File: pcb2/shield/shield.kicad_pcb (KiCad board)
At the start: 2 copper layers, 48.4 x 50 mm, 17 parts, among them IC1 AM26C31CNSR, IC2 AM26C31CNSR, P1 ARD_NW, P10 BUS5, P11 BUS6, P12 BUS7, P13 BUS8, P2 ARD_SW, P3 ARD_NE, P4 ARD_SE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

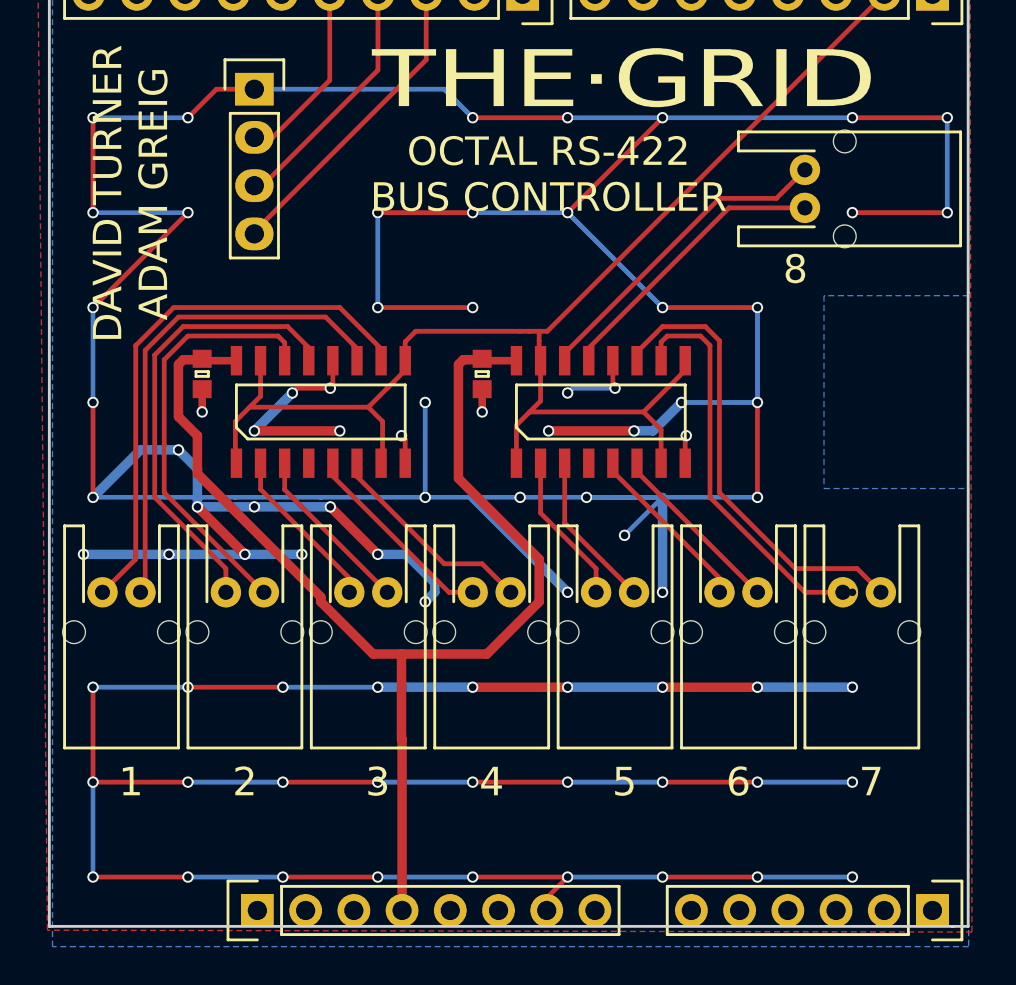
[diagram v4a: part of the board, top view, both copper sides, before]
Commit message: Changed vias from 0.6/0.4 to 0.6/0.3
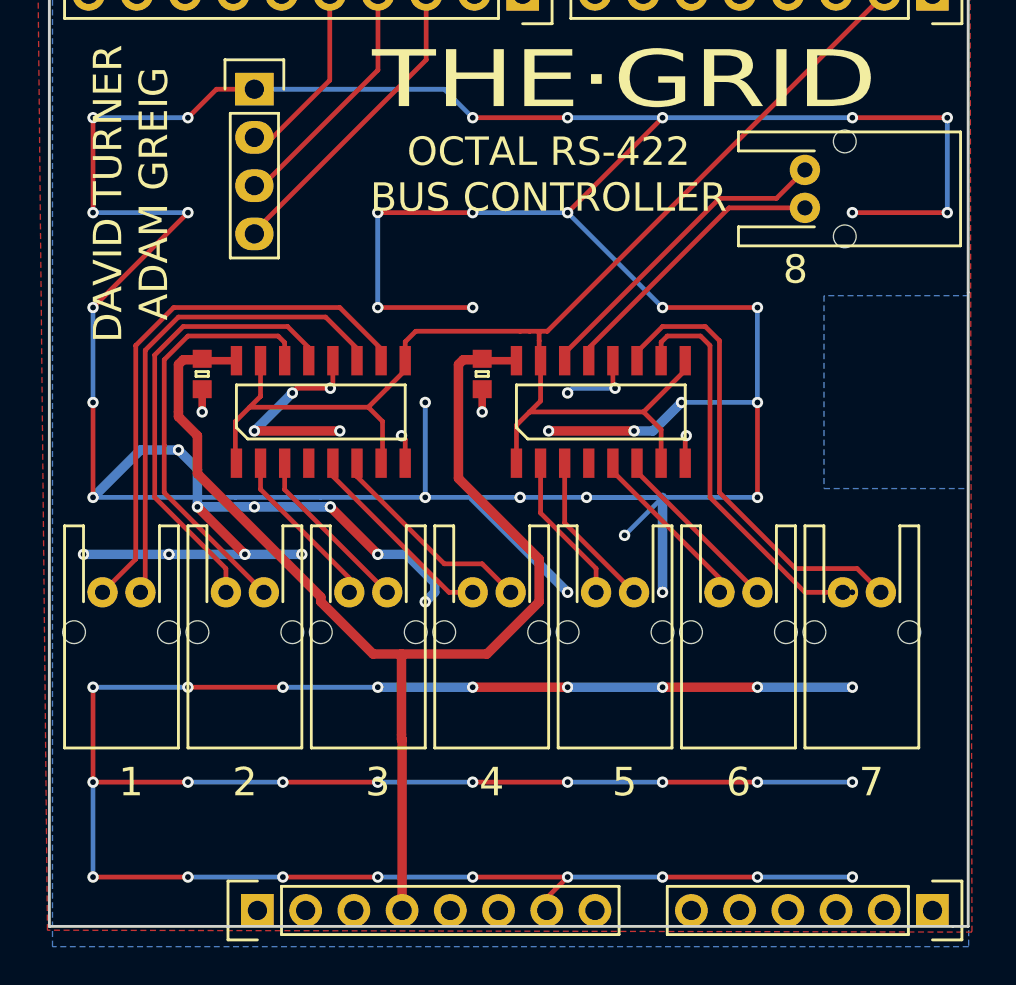
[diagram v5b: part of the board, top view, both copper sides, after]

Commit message: set mask clearance to 0 and regen gerbers
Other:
- rule pad_to_mask_clearance: 0.2 -> 0
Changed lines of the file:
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@@
-(kicad_pcb (version 4) (host pcbnew 4.0.2-4+6225~38~ubuntu15.10.1-stable)
+(kicad_pcb (version 4) (host pcbnew 0.201601071449+6428~40~ubuntu14.04.1-stable)
   (general
     (links 40)
@@
     (pad_size 1.524 1.524)
     (pad_drill 0.762)
-    (pad_to_mask_clearance 0.2)
+    (pad_to_mask_clearance 0)
     (aux_axis_origin 0 0)
     (visible_elements FFFFFF7F)
     (pcbplotparams
-      (layerselection 0x010f8_80000001)
+      (layerselection 0x010f8_ffffffff)
       (usegerberextensions true)
       (excludeedgelayer true)

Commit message: Repsin of new shield PCB, nominal first route.
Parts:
- removed P1: ARD_NW, Pin_Headers:Pin_Header_Straight_1x08
- removed P2: ARD_SW, Pin_Headers:Pin_Header_Straight_1x06
- removed P3: ARD_NE, Pin_Headers:Pin_Header_Straight_1x10
- removed P4: ARD_SE, Pin_Headers:Pin_Header_Straight_1x08
- added C10: 1u, agg:0603, F.Cu at (90.2, 106.2)
- added C3: 100n, agg:0603, F.Cu at (106.0, 87.6)
- added C4: 10u, agg:0603, F.Cu at (106.0, 86.0)
- added C5: C, agg:0603, F.Cu at (102.6, 86.8)
- added C6: 100n, agg:0603, F.Cu at (101.1, 86.8)
- added C7: 1u, agg:0603, F.Cu at (99.6, 86.8)
- added C8: 100n, agg:0603, F.Cu at (97.8, 99.8)
- added C9: 1u, agg:0603, F.Cu at (93.5, 103.7)
- added IC3: AM26C31, agg:SOIC-16, F.Cu at (81.0, 92.1)
- added IC4: AM26C31, agg:SOIC-16, F.Cu at (87.6, 80.7)
- added J1: MICROUSB, agg:MICROUSB_MOLEX_47589-0001, F.Cu at (100.4, 108.4)
- added P?: SWD_TC, agg:TC2030-NL, F.Cu at (107.4, 100.6)
- IC1: value AM26C31CNSR -> STM32F0xxKxTx; footprint agg:SOIC-16 -> agg:LQFP-32
- IC2: value AM26C31CNSR -> MCP1700; footprint agg:SOIC-16 -> agg:SOT-23
- moved P12 38.9 mm to (76.5, 69.1), turned to 0 degrees
- moved P5 37.8 mm to (76.7, 106.2), turned to 90 degrees
- moved P11 30.2 mm to (83.5, 69.1), turned to 0 degrees
- moved IC1 26.2 mm to (101.9, 93.8), turned to 270 degrees
- moved P10 26.0 mm to (90.5, 69.1), turned to 0 degrees
- moved P7 25.1 mm to (69.1, 76.5), turned to 90 degrees
- moved IC2 20.8 mm to (93.2, 106.2), turned to 0 degrees
- moved C2 17.1 mm to (79.0, 98.5), turned to 0 degrees
- moved P8 11.8 mm to (69.1, 83.5), turned to 90 degrees
- moved P6 10.7 mm to (69.1, 97.5), turned to 90 degrees
- moved C1 8.51 mm to (94.0, 83.0), turned to 90 degrees
- moved P13 6.83 mm to (97.5, 69.1), turned to 0 degrees
- moved P9 5.95 mm to (69.1, 90.5), turned to 90 degrees
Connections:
- IC1 pad 1: /TX -> +3V3
- IC1 pad 11: Net-(IC1-Pad11) -> /SHIFT_RCK
- IC1 pad 12: GND -> /SHIFT_SRCK
- IC1 pad 13: Net-(IC1-Pad13) -> /SHIFT_DATA
- IC1 pad 15: /TX -> Net-(IC1-Pad15)
- IC1 pad 16: +5V -> GND
- IC1 pad 4: (no net) -> /nRST
- IC1 pad 5: Net-(IC1-Pad5) -> +3V3
- IC1 pad 7: /TX -> Net-(IC1-Pad7)
- IC1 pad 8: GND -> /TX
- IC1 pad 9: /TX -> Net-(IC1-Pad9)
- IC2 pad 1: /TX -> GND
- IC2 pad 2: Net-(IC2-Pad2) -> +3V3
- IC2 pad 3: Net-(IC2-Pad3) -> +5V
- P10 pad 1: Net-(IC2-Pad2) -> Net-(IC4-Pad2)
- P10 pad 2: Net-(IC2-Pad3) -> Net-(IC4-Pad3)
- P11 pad 1: Net-(IC2-Pad5) -> Net-(IC4-Pad6)
- P11 pad 2: Net-(IC2-Pad6) -> Net-(IC4-Pad5)
- P12 pad 1: Net-(IC2-Pad10) -> Net-(IC4-Pad10)
- P12 pad 2: Net-(IC2-Pad11) -> Net-(IC4-Pad11)
- P13 pad 1: Net-(IC2-Pad13) -> Net-(IC4-Pad14)
- P13 pad 2: Net-(IC2-Pad14) -> Net-(IC4-Pad13)
- P6 pad 1: Net-(IC1-Pad2) -> Net-(IC3-Pad2)
- P6 pad 2: Net-(IC1-Pad3) -> Net-(IC3-Pad3)
- P7 pad 1: Net-(IC1-Pad5) -> Net-(IC3-Pad6)
- P7 pad 2: Net-(IC1-Pad6) -> Net-(IC3-Pad5)
- P8 pad 1: Net-(IC1-Pad10) -> Net-(IC3-Pad10)
- P8 pad 2: Net-(IC1-Pad11) -> Net-(IC3-Pad11)
- P9 pad 1: Net-(IC1-Pad13) -> Net-(IC3-Pad14)
- P9 pad 2: Net-(IC1-Pad14) -> Net-(IC3-Pad13)
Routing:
- net GND: track 395.0 -> 30.1 mm, vias 80 -> 19
- net +3V3: track 0.00 -> 81.0 mm, vias 0 -> 2
- net /SHIFT_RCK: track 9.75 -> 56.8 mm, vias 0 -> 2
- net /SHIFT_SRCK: track 13.1 -> 49.0 mm, vias 0 -> 2
- net Net-(IC3-Pad5): track 0.00 -> 34.7 mm
- net /TX: track 73.6 -> 104.4 mm
- net Net-(IC1-Pad10): track 29.0 -> 0.00 mm
- net Net-(IC1-Pad11): track 26.1 -> 0.00 mm
- net Net-(IC3-Pad6): track 0.00 -> 24.6 mm
- net Net-(IC2-Pad11): track 24.3 -> 0.00 mm
- net Net-(IC1-Pad13): track 23.9 -> 0.00 mm
- net Net-(IC3-Pad3): track 0.00 -> 23.7 mm
- net /SHIFT_DATA: track 16.4 -> 39.7 mm, vias 0 -> 2
- net Net-(IC4-Pad11): track 0.00 -> 23.1 mm
- net Net-(IC1-Pad14): track 22.4 -> 0.00 mm
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- removed copper zone on F.Cu, net GND
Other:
- board size 48.4 x 50 mm -> 50 x 50 mm
- board text removed: "-TX"
- board text removed: "1"
- board text removed: "2"
- board text removed: "3"
- board text removed: "4"
- board text removed: "5"
- board text removed: "6"
- board text removed: "7"
- board text removed: "8"

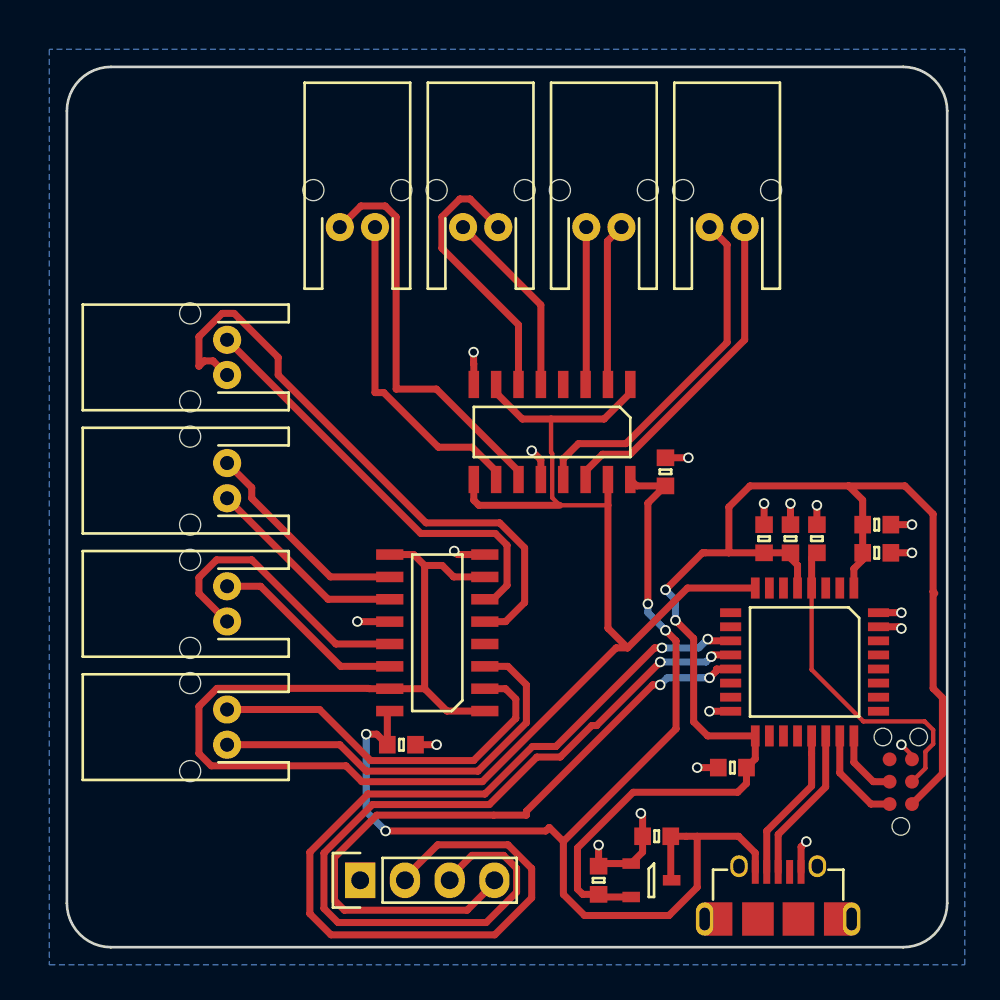
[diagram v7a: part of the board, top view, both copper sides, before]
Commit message: Re-route of shield, DRC issues though.
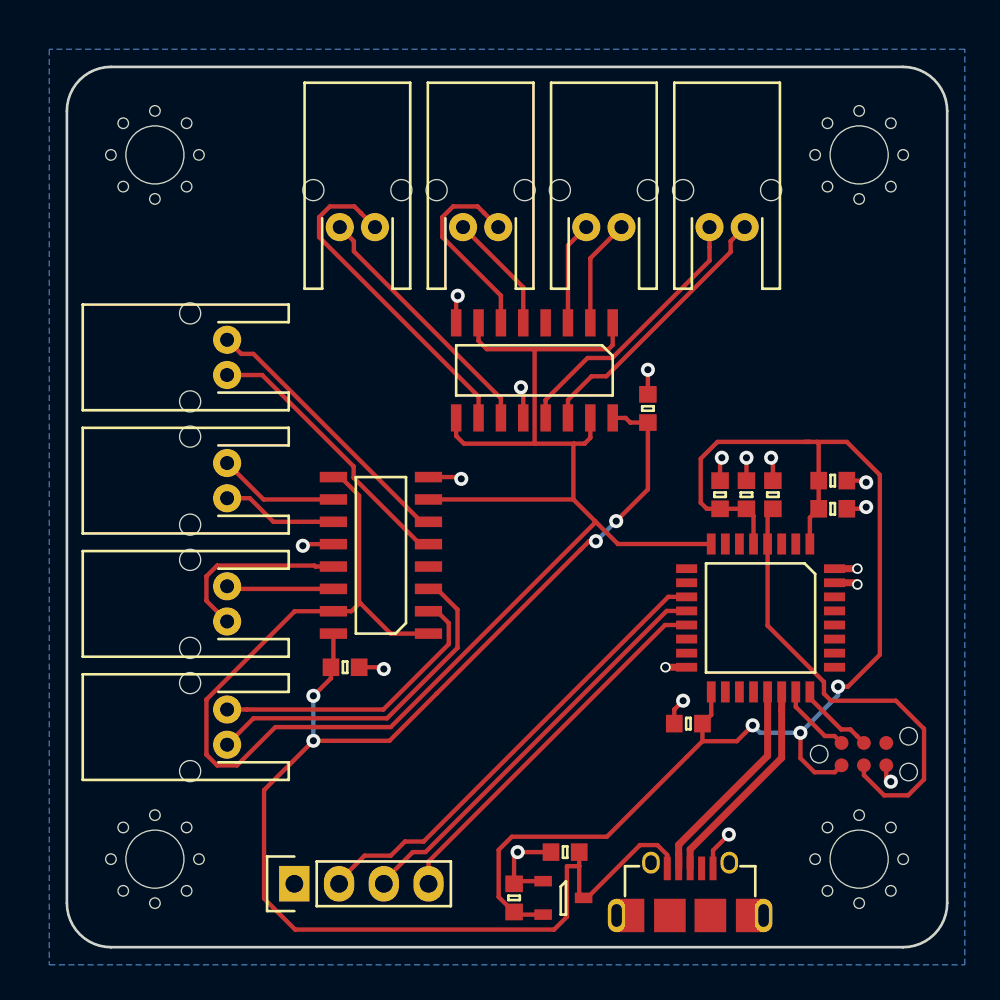
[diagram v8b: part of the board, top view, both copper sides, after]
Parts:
- removed P?: SWD_TC, agg:TC2030-NL
- added P1: SWD_TC, agg:TC2030-NL, F.Cu at (105.3, 99.0)
- added X1: PART, agg:M3_MOUNT, F.Cu at (65.0, 105.0)
- added X2: PART, agg:M3_MOUNT, F.Cu at (105.0, 105.0)
- added X3: PART, agg:M3_MOUNT, F.Cu at (105.0, 65.0)
- added X4: PART, agg:M3_MOUNT, F.Cu at (65.0, 65.0)
- moved C2 5.44 mm to (75.8, 94.1)
- moved IC3 5.44 mm to (77.8, 87.7)
- moved C9 5.28 mm to (88.3, 104.6)
- moved IC2 5.10 mm to (88.2, 107.2)
- moved J1 5.00 mm to (95.4, 108.2)
- moved C10 4.90 mm to (85.4, 107.2)
- moved P5 3.75 mm to (72.9, 106.4)
- moved C1 3.74 mm to (93.0, 79.4)
- moved IC4 3.64 mm to (86.6, 77.2)
- moved C3 3.54 mm to (103.5, 85.1)
- moved C4 3.54 mm to (103.5, 83.5)
- moved C5 3.54 mm to (100.1, 84.3)
- moved C6 3.54 mm to (98.6, 84.3)
- moved C7 3.54 mm to (97.1, 84.3)
- moved C8 3.54 mm to (95.3, 97.3)
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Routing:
- net /SHIFT_RCK: track 56.8 -> 26.6 mm, vias 2 -> 0
- net /SHIFT_SRCK: track 49.0 -> 23.7 mm, vias 2 -> 0
- net Net-(IC3-Pad5): track 34.7 -> 15.8 mm
- net /SHIFT_DATA: track 39.7 -> 21.5 mm, vias 2 -> 0
- net +5V: track 69.5 -> 79.1 mm
- net Net-(IC3-Pad6): track 24.6 -> 15.7 mm
- net Net-(IC4-Pad11): track 23.1 -> 14.6 mm
- net /nRST: track 18.5 -> 26.2 mm
- net +3V3: track 81.0 -> 75.1 mm, vias 2 -> 3
- net Net-(IC3-Pad13): track 16.4 -> 10.5 mm
- net Net-(IC3-Pad10): track 12.3 -> 6.89 mm
- net Net-(IC3-Pad14): track 11.1 -> 6.10 mm
- net Net-(IC3-Pad11): track 11.6 -> 6.59 mm
- net Net-(IC3-Pad2): track 21.7 -> 16.8 mm
- net Net-(IC4-Pad13): track 20.2 -> 15.5 mm
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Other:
- net class Default: clearance 0.2 -> 0.25; via_dia 0.6 -> 0.8
- rule trace_clearance: 0.2 -> 0.25
- rule via_min_drill: 0.3 -> 0.4
- rule via_min_size: 0.4 -> 0.8
